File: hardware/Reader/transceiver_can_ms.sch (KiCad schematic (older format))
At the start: 9 parts, among them IC5 MCP2562-H_MF

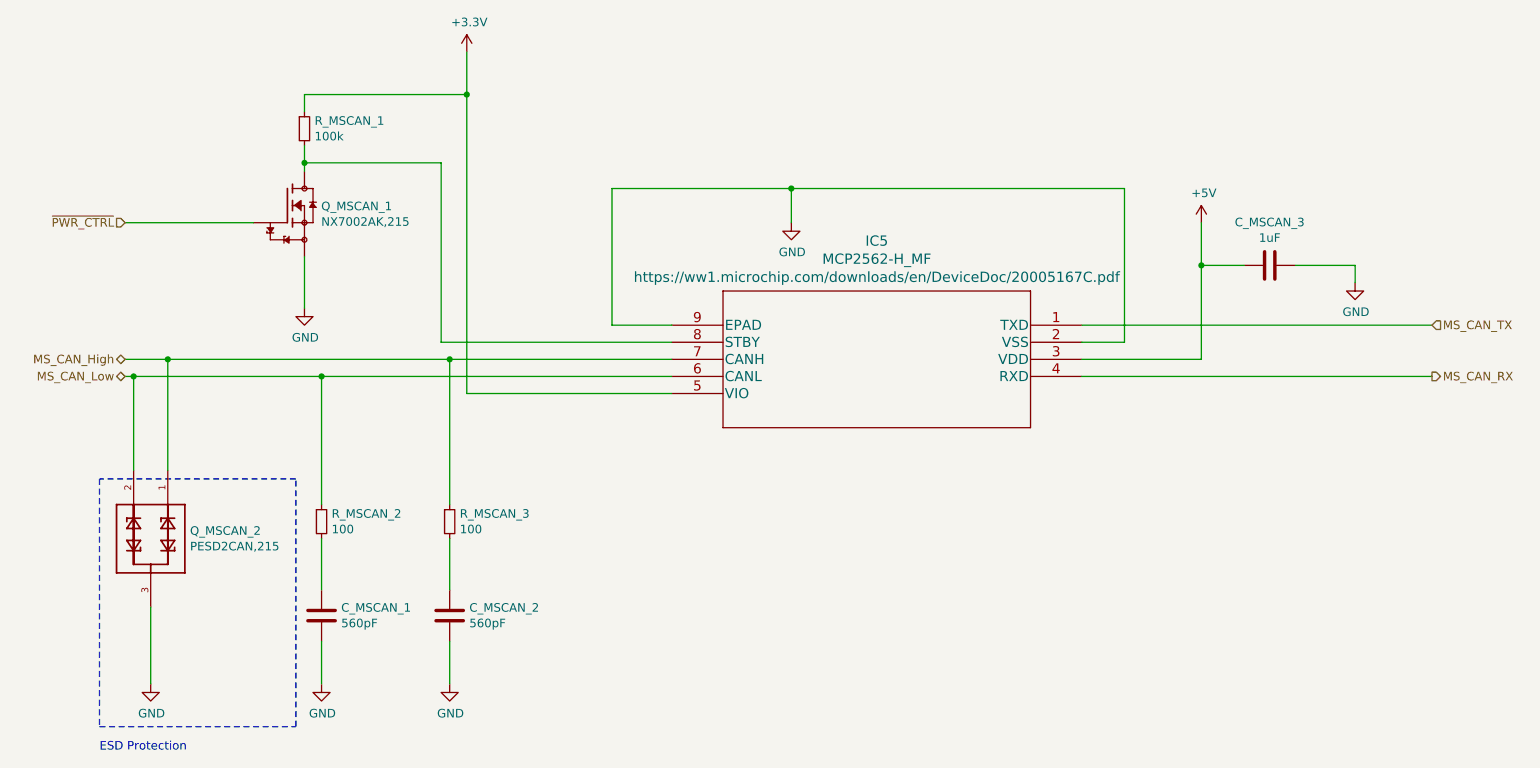
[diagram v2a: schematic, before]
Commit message: Added ESD Protection. Fixed minor bugs on schematic. Attempted placement of components
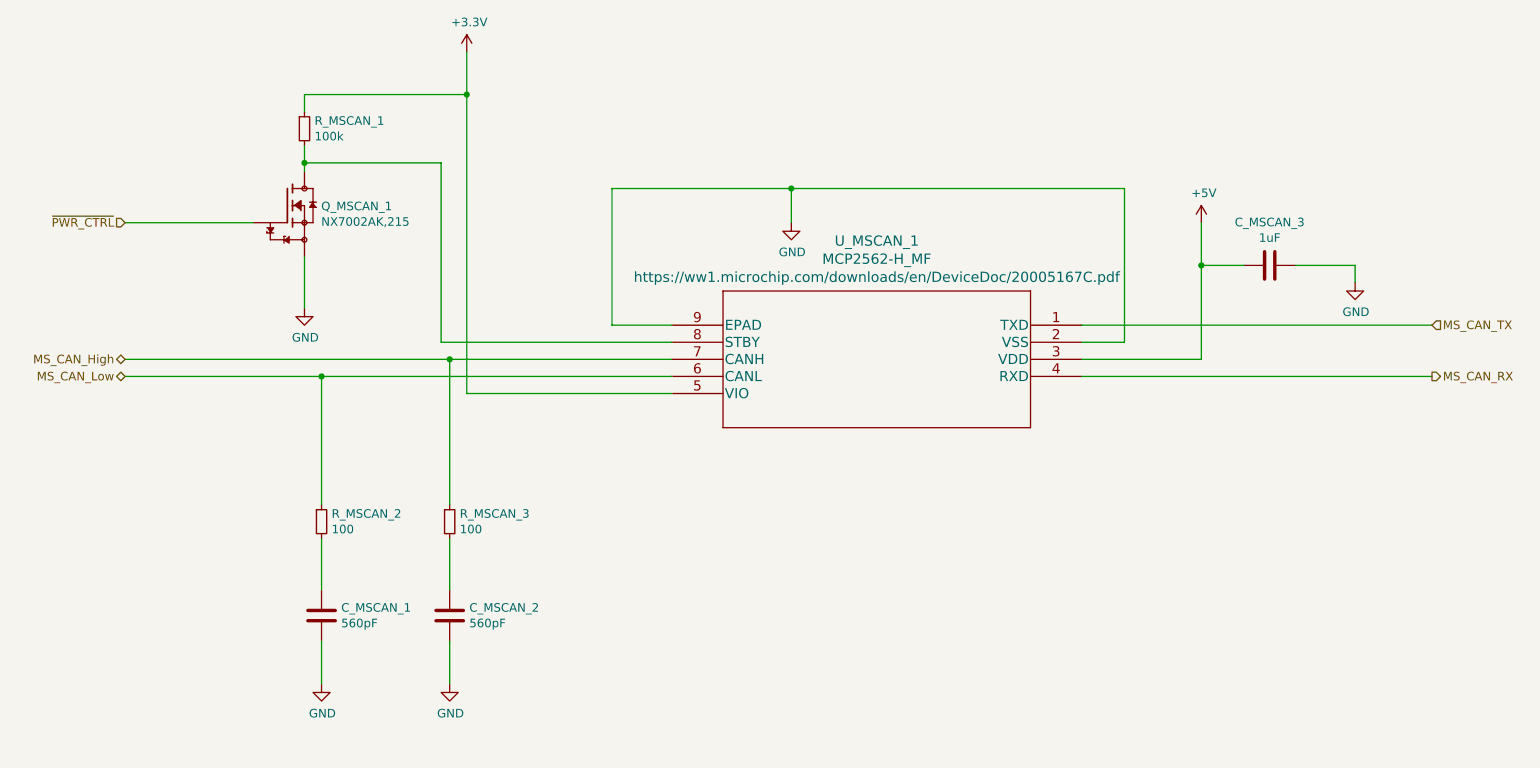
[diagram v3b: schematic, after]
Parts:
- removed Q_MSCAN_2: PESD2CAN,215, footprints:SOT95P230X110-3N, symbol PESD2CAN_215:PESD2CAN,215
- renumbered IC5 to U_MSCAN_1
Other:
- note removed: "ESD Protection"
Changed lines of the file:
@@
 $Descr USLetter 11000 8500
 encoding utf-8
-Sheet 11 18
+Sheet 6 19
 Title "CANnect Reader | Medium Speed CAN Transceiver"
-Date "2020-10-20"
-Rev "0.0.01"
+Date "2020-10-25"
+Rev "0.0.03"
 Comp "CANtech"
 Comment1 "Created by Choong Jin Ng | jin8383@gmail.com"
@@
 MS_CAN_Low
 $Comp
-L PESD2CAN_215:PESD2CAN,215 D?
-U 1 1 5FB39FD5
-P 1750 4050
-AR Path="/5F95F80B/5FAEE035/5FB39FD5" Ref="D?"  Part="1"
-AR Path="/5F95F80B/5FB34A7C/5FB39FD5" Ref="Q_MSCAN_2"  Part="1"
-F 0 "Q_MSCAN_2" V 1704 4280 50  0000 L CNN
-F 1 "PESD2CAN,215" V 1795 4280 50  0000 L CNN
-F 2 "footprints:SOT95P230X110-3N" H 1750 4050 50  0001 L BNN
-F 3 "https://assets.nexperia.com/documents/data-sheet/PESD2CAN.pdf" H 1750 4050 50  0001 L BNN
-	1    1750 4050
-	0    1    1    0
-$EndComp
-Wire Wire Line
-	1600 3000 1850 3000
-$Comp
-L power:GND #PWR?
-U 1 1 5FB39FDC
-P 1750 4900
-AR Path="/5F95F80B/5FAEE035/5FB39FDC" Ref="#PWR?"  Part="1"
-AR Path="/5F95F80B/5FB34A7C/5FB39FDC" Ref="#PWR0157"  Part="1"
-F 0 "#PWR0157" H 1750 4650 50  0001 C CNN
-F 1 "GND" H 1755 4727 50  0000 C CNN
-F 2 "" H 1750 4900 50  0001 C CNN
-F 3 "" H 1750 4900 50  0001 C CNN
-	1    1750 4900
-	1    0    0    -1
-$EndComp
-Wire Wire Line
-	1750 4450 1750 4900
-Wire Notes Line
-	1450 5150 2600 5150
-Wire Notes Line
-	2600 5150 2600 3700
-Wire Notes Line
-	2600 3700 1450 3700
-Wire Notes Line
-	1450 3700 1450 5150
-Text Notes 1450 5300 0    50   ~ 0
-ESD Protection
-$Comp
 L MCP2562HMF:MCP2562-H_MF IC?
 U 1 1 5FB39FE8
 P 7200 2800
 AR Path="/5F95F80B/5FAEE035/5FB39FE8" Ref="IC?"  Part="1"
-AR Path="/5F95F80B/5FB34A7C/5FB39FE8" Ref="IC5"  Part="1"
-F 0 "IC5" H 8400 3293 60  0000 C CNN
+AR Path="/5F95F80B/5FB34A7C/5FB39FE8" Ref="U_MSCAN_1"  Part="1"
+F 0 "U_MSCAN_1" H 8400 3293 60  0000 C CNN
 F 1 "MCP2562-H_MF" H 8400 3187 60  0000 C CNN
 F 2 "footprints:MCP2562-H&slash_MF" H 8400 3040 60  0001 C CNN
@@
 	-1   0    0    -1
 $EndComp
-Wire Wire Line
-	1650 3100 1650 3650
-Connection ~ 1650 3100
-Wire Wire Line
-	1650 3100 1600 3100
-Connection ~ 1850 3000
-Wire Wire Line
-	1850 3000 1850 3650
 $Comp
 L Device:R_Small R?
@@
 	2750 3850 2750 3100
 Connection ~ 2750 3100
-Wire Wire Line
-	1650 3100 2750 3100
 Wire Wire Line
 	7200 2900 7450 2900
@@
 MS_CAN_RX
 Wire Wire Line
-	1850 3000 3500 3000
-Wire Wire Line
 	3500 3850 3500 3000
 Connection ~ 3500 3000
 Wire Wire Line
 	3500 3000 4800 3000
+Wire Wire Line
+	1600 3100 2750 3100
+Wire Wire Line
+	1600 3000 3500 3000
 $EndSCHEMATC

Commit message: Fixed bugs on the reader schematic. Exported Schematic Electrical report
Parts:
- C_MSCAN_1, C_MSCAN_2: Manufacturer (none) -> Yageo; Part Name (none) -> CC0603KRX7R9BB561; Vendor (none) -> DigiKey Canada; digikeypn (none) -> 311-1079-1-ND
- C_MSCAN_3: Manufacturer (none) -> Kermet; Part Name (none) -> C0603C105K4RACTU; Vendor (none) -> DigiKey Canada; digikeypn (none) -> 399-7847-1-ND
- Q_MSCAN_1: Manufacturer (none) -> Nexperia USA Inc.; Part Name (none) -> NX7002AK,215; Vendor (none) -> DigiKey Canada; digikeypn (none) -> 1727-1289-1-ND
- R_MSCAN_1: Manufacturer (none) -> Yageo; Vendor (none) -> DigiKey Canada; digikeypn (none) -> 311-2395-1-ND
- R_MSCAN_2, R_MSCAN_3: Manufacturer (none) -> Panasonic Electronic Components; Vendor (none) -> DigiKey Canada; digikeypn (none) -> P100FCT-ND
- U_MSCAN_1: Manufacturer (none) -> Microchip Technology; Part Name (none) -> MCP2562-H_MF; Vendor (none) -> DigiKey Canada; digikeypn (none) -> MCP2562-H/MF-ND
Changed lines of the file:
@@
 F 2 "footprints:MCP2562-H&slash_MF" H 8400 3040 60  0001 C CNN
 F 3 "https://ww1.microchip.com/downloads/en/DeviceDoc/20005167C.pdf" H 8400 3081 60  0000 C CNN
+F 4 "MCP2562-H_MF" H 7200 2800 50  0001 C CNN "Part Name"
+F 5 "Microchip Technology" H 7200 2800 50  0001 C CNN "Manufacturer"
+F 6 "DigiKey Canada" H 7200 2800 50  0001 C CNN "Vendor"
+F 7 "MCP2562-H/MF-ND" H 7200 2800 50  0001 C CNN "digikeypn"
 	1    7200 2800
 	-1   0    0    -1
@@
 F 3 "https://industrial.panasonic.com/cdbs/www-data/pdf/RDA0000/AOA0000C304.pdf" H 2750 3950 50  0001 C CNN
 F 4 "ERJ-8ENF1000V" H 2750 3950 50  0001 C CNN "Part Name"
+F 5 "DigiKey Canada" H 2750 3950 50  0001 C CNN "Vendor"
+F 6 "Panasonic Electronic Components" H 2750 3950 50  0001 C CNN "Manufacturer"
+F 7 "P100FCT-ND" H 2750 3950 50  0001 C CNN "digikeypn"
 	1    2750 3950
 	1    0    0    -1
@@
 F 3 "https://industrial.panasonic.com/cdbs/www-data/pdf/RDA0000/AOA0000C304.pdf" H 3500 3950 50  0001 C CNN
 F 4 "ERJ-8ENF1000V" H 3500 3950 50  0001 C CNN "Part Name"
+F 5 "DigiKey Canada" H 3500 3950 50  0001 C CNN "Vendor"
+F 6 "Panasonic Electronic Components" H 3500 3950 50  0001 C CNN "Manufacturer"
+F 7 "P100FCT-ND" H 3500 3950 50  0001 C CNN "digikeypn"
 	1    3500 3950
 	1    0    0    -1
@@
 F 2 "footprints:CAPC1608X90" H 2788 4350 50  0001 C CNN
 F 3 "https://www.yageo.com/upload/media/product/productsearch/datasheet/mlcc/UPY-GPHC_X7R_6.3V-to-50V_18.pdf" H 2750 4500 50  0001 C CNN
+F 4 "CC0603KRX7R9BB561" H 2750 4500 50  0001 C CNN "Part Name"
+F 5 "Yageo" H 2750 4500 50  0001 C CNN "Manufacturer"
+F 6 "DigiKey Canada" H 2750 4500 50  0001 C CNN "Vendor"
+F 7 "311-1079-1-ND" H 2750 4500 50  0001 C CNN "digikeypn"
 	1    2750 4500
 	1    0    0    -1
@@
 F 2 "footprints:CAPC1608X90" H 3538 4350 50  0001 C CNN
 F 3 "https://www.yageo.com/upload/media/product/productsearch/datasheet/mlcc/UPY-GPHC_X7R_6.3V-to-50V_18.pdf" H 3500 4500 50  0001 C CNN
+F 4 "CC0603KRX7R9BB561" H 3500 4500 50  0001 C CNN "Part Name"
+F 5 "Yageo" H 3500 4500 50  0001 C CNN "Manufacturer"
+F 6 "DigiKey Canada" H 3500 4500 50  0001 C CNN "Vendor"
+F 7 "311-1079-1-ND" H 3500 4500 50  0001 C CNN "digikeypn"
 	1    3500 4500
 	1    0    0    -1
@@
 F 5 "7" H 2550 2100 50  0001 L BNN "Field5"
 F 6 "IPC-7351B" H 2550 2100 50  0001 L BNN "Field6"
+F 7 "NX7002AK,215" H 2550 2100 50  0001 C CNN "Part Name"
+F 8 "Nexperia USA Inc." H 2550 2100 50  0001 C CNN "Manufacturer"
+F 9 "DigiKey Canada" H 2550 2100 50  0001 C CNN "Vendor"
+F 10 "1727-1289-1-ND" H 2550 2100 50  0001 C CNN "digikeypn"
 	1    2550 2100
 	1    0    0    -1
@@
 F 3 "https://www.yageo.com/upload/media/product/productsearch/datasheet/rchip/PYu-RT_1-to-0.01_RoHS_L_12.pdf" H 2650 1650 50  0001 C CNN
 F 4 "RT0603DRE07100KL" H 2650 1650 50  0001 C CNN "Part Name"
+F 5 "Yageo" H 2650 1650 50  0001 C CNN "Manufacturer"
+F 6 "DigiKey Canada" H 2650 1650 50  0001 C CNN "Vendor"
+F 7 "311-2395-1-ND" H 2650 1650 50  0001 C CNN "digikeypn"
 	1    2650 1650
 	1    0    0    -1
@@
 F 2 "footprints:0603" H 8338 2300 50  0001 C CNN
 F 3 "https://content.kemet.com/datasheets/KEM_C1002_X7R_SMD.pdf" H 8300 2450 50  0001 C CNN
+F 4 "C0603C105K4RACTU" H 8300 2450 50  0001 C CNN "Part Name"
+F 5 "Kermet" H 8300 2450 50  0001 C CNN "Manufacturer"
+F 6 "DigiKey Canada" H 8300 2450 50  0001 C CNN "Vendor"
+F 7 "399-7847-1-ND" H 8300 2450 50  0001 C CNN "digikeypn"
 	1    8300 2450
 	0    1    1    0
